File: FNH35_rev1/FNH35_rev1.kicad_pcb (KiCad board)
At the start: 2 copper layers, 13 x 7.7 mm, 118 parts, among them J1 Conn_01x03, J2 Conn_01x21, J3 DX07B024JJ3R1600, K0 KEYSW, K1 KEYSW, K10 KEYSW, K11 KEYSW, K12 KEYSW, K2 KEYSW, K20 KEYSW, K21 KEYSW, K22 KEYSW, K23 KEYSW, K30 KEYSW, K31 KEYSW, K32 KEYSW, K33 KEYSW, K40 KEYSW, K41 KEYSW, K42 KEYSW, K43 KEYSW, SW1 SW_PUSH, U1 STM32F303CCTx, U2 LD1117S33TR_SOT223, U3 74AHCT125, X1 XTAL_GND

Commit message: more pcb layouting, decided to get rid of fuse in next step
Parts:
- CB0, CB1, CB10, CB11, CB12, CB2, CB20, CB21, CB22, CB23, CB30, CB31, CB32, CB33, CB40, CB41, CB42, CB43, CU1, CU2, CU3, CU4, CU5, CU6, CU7, CU8, DS0, DS1, DS10, DS11, DS12, DS2, DS20, DS21, DS22, DS23, DS30, DS31, DS32, DS33, DS40, DS41, DS42, DS43, DU1, DU2, DU3, DU4, DU5, DU6, DU7, DU8, J2, J3: moved to B.Cu
- moved U2 194.3 mm to (26.2, 38.1), turned to 180 degrees
- moved C9 192.0 mm to (33.3, 31.0)
- moved C10 183.7 mm to (65.4, 21.4)
- moved C4 183.6 mm to (26.2, 45.2), turned to 90 degrees
- moved C3 182.9 mm to (33.3, 33.3)
- moved J3 179.5 mm to (27.1, 26.2)
- moved C11 162.1 mm to (26.2, 59.5), turned to 180 degrees
- moved X1 162.1 mm to (31.0, 87.3)
- moved U1 162.0 mm to (31.0, 73.8), turned to 90 degrees
- moved C1 156.6 mm to (40.5, 95.2), turned to 315 degrees
- moved C8 156.5 mm to (39.3, 69.1)
- moved C7 156.0 mm to (26.2, 64.3), turned to 90 degrees
- moved C2 154.6 mm to (45.2, 90.5), turned to 315 degrees
- moved C6 154.2 mm to (21.4, 78.6), turned to 180 degrees
- moved C5 153.7 mm to (24.9, 81.0), turned to 180 degrees
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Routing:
- added copper zone on B.Cu, net GNDD
- added copper zone on F.Cu, net GNDD
- removed copper zone on B.Cu, net +5V
- removed copper zone on F.Cu, net GND
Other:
- outline, holes or cut-outs redrawn

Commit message: almost done
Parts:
- removed F1: Polyfuse_Small, Capacitors_SMD:C_0805_HandSoldering
- removed JP1: , Wire_Connections_Bridges:WireConnection_1.00mmDrill
- C10, C3, C4, C9, D1, J1, R1, R2, U2: moved to B.Cu
- moved J1 187.7 mm to (26.2, 28.6), turned to 180 degrees
- moved R6 165.8 mm to (39.8, 74.6)
- moved D1 160.2 mm to (41.5, 32.4), turned to 45 degrees
- moved R7 157.1 mm to (41.2, 78.4), turned to 180 degrees
- moved R2 140.2 mm to (47.4, 35.2), turned to 180 degrees
- moved R1 140.0 mm to (47.5, 37.8), turned to 180 degrees
- moved U3 133.1 mm to (36.9, 40.3)
- moved SW1 118.1 mm to (22.1, 79.7), turned to 90 degrees
- moved R5 117.6 mm to (20.9, 87.3), turned to 180 degrees
- moved R3 112.1 mm to (8.02, 95.2)
- moved R4 111.9 mm to (1.03, 95.2)
- moved C10 33.9 mm to (33.5, 32.7), turned to 90 degrees
- moved C5 19.5 mm to (20.8, 61.9), turned to 270 degrees
- moved J3 16.7 mm to (43.7, 26.2)
- moved C1 16.2 mm to (27.1, 86.0)
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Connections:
- C1 pad 2: GNDD -> GND
- C11 pad 2: GNDD -> GND
- C12 pad 2: GNDD -> GND
- C2 pad 2: GNDD -> GND
- C3 pad 2: GNDD -> GND
- C4 pad 2: GNDD -> GND
- C5 pad 2: GNDD -> GND
- C6 pad 2: GNDD -> GND
- C7 pad 2: GNDD -> GND
- C8 pad 2: GNDD -> GND
- C9 pad 2: GNDD -> GND
- D1 pad 4: Net-(D1-Pad4) -> +5V
- J2 pad 13: Net-(J2-Pad13) -> /DA-
- J2 pad 14: Net-(J2-Pad14) -> /DA+
- J2 pad 20: GNDD -> GND
- J3 pad A4: Net-(D1-Pad4) -> +5V
- J3 pad A9: Net-(D1-Pad4) -> +5V
- J3 pad B4: Net-(D1-Pad4) -> +5V
- J3 pad B9: Net-(D1-Pad4) -> +5V
- R5 pad 2: GNDD -> GND
- U1 pad 23: GNDD -> GND
- U1 pad 32: Net-(J2-Pad13) -> /DA-
- U1 pad 33: Net-(J2-Pad14) -> /DA+
- U1 pad 35: GNDD -> GND
- U1 pad 47: GNDD -> GND
- U1 pad 8: GNDD -> GND
- U2 pad 1: GNDD -> GND
- X1 pad 3: GNDD -> GND
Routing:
- net +5V: track 0.00 -> 539.2 mm, vias 0 -> 30
- net GND: track 0.00 -> 538.5 mm, vias 0 -> 36
- net /SwitchMatrix/col3: track 0.00 -> 203.6 mm, vias 0 -> 7
- net /SwitchMatrix/col2: track 0.00 -> 183.9 mm, vias 0 -> 8
- net /SwitchMatrix/col0: track 0.00 -> 150.3 mm, vias 0 -> 7
- net /SwitchMatrix/row0: track 0.00 -> 141.8 mm, vias 0 -> 3
- net /SwitchMatrix/row1: track 0.00 -> 139.5 mm, vias 0 -> 1
- net /SwitchMatrix/col4: track 0.00 -> 136.4 mm, vias 0 -> 3
- net /SwitchMatrix/row2: track 0.00 -> 132.5 mm, vias 0 -> 1
- net /SwitchMatrix/row3: track 0.00 -> 85.2 mm, vias 0 -> 1
- net +3V3: track 0.00 -> 82.8 mm, vias 0 -> 1
- net Net-(DB23-Pad1): track 0.00 -> 60.5 mm
- net /SwitchMatrix/col1: track 0.00 -> 44.3 mm, vias 0 -> 4
- net Net-(DB11-Pad6): track 0.00 -> 43.8 mm, vias 0 -> 2
- net Net-(DB23-Pad6): track 0.00 -> 36.9 mm
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- added copper zone on B.Cu, net GND
- added copper zone on F.Cu, net GND
- removed copper zone on B.Cu, net GNDD
- removed copper zone on F.Cu, net GNDD
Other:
- outline, holes or cut-outs redrawn

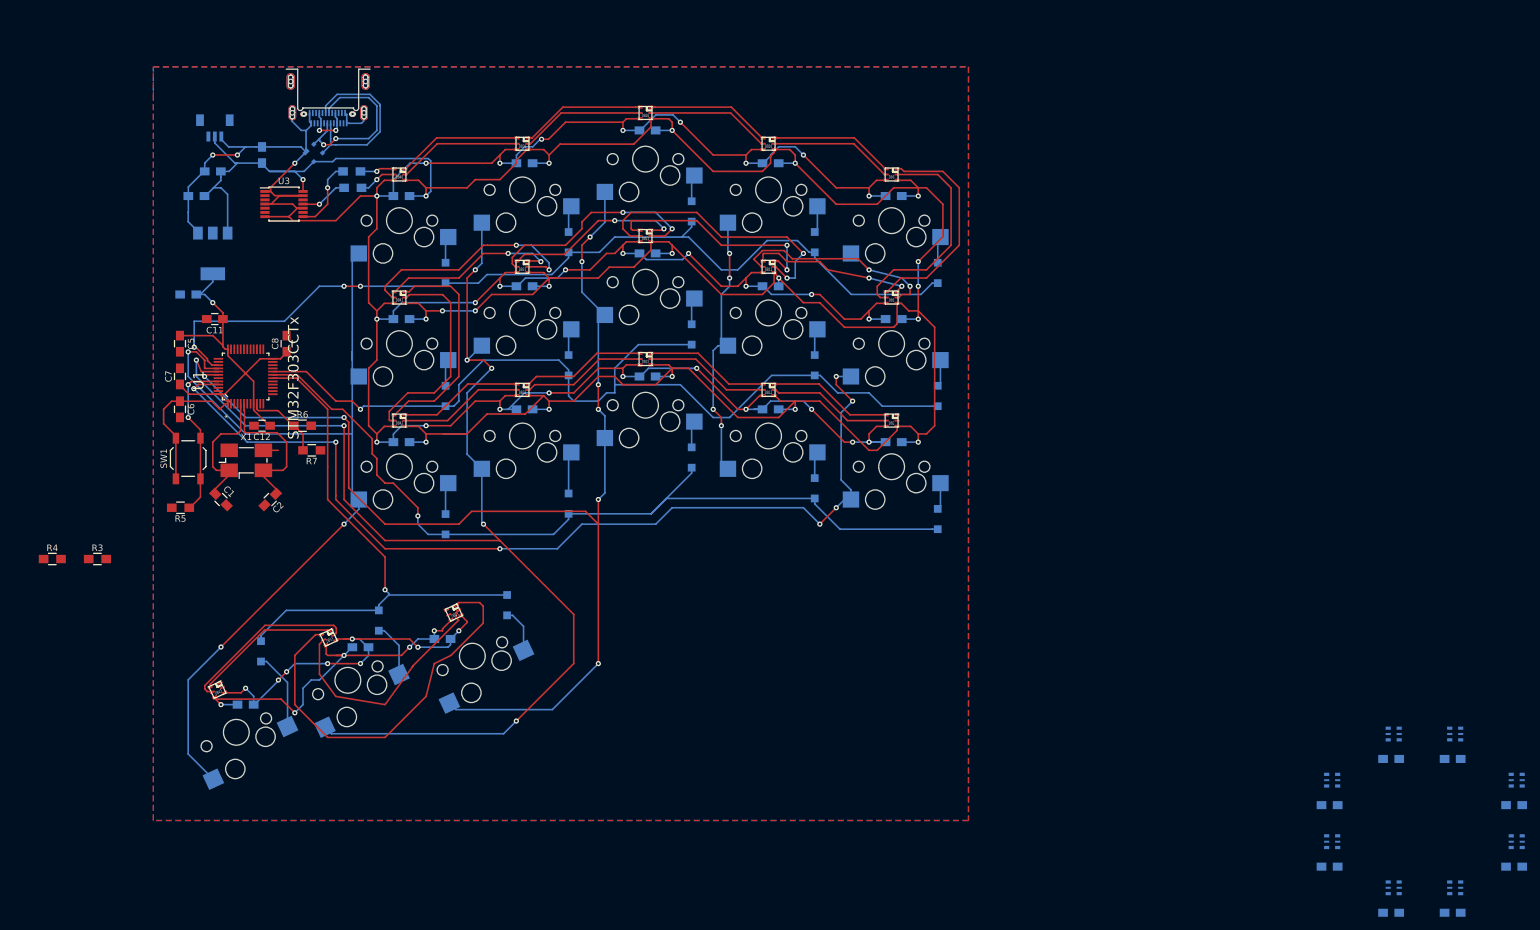
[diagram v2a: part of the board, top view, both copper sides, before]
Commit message: noticed the diodes are conflicting with the sockets, deleting traces from here
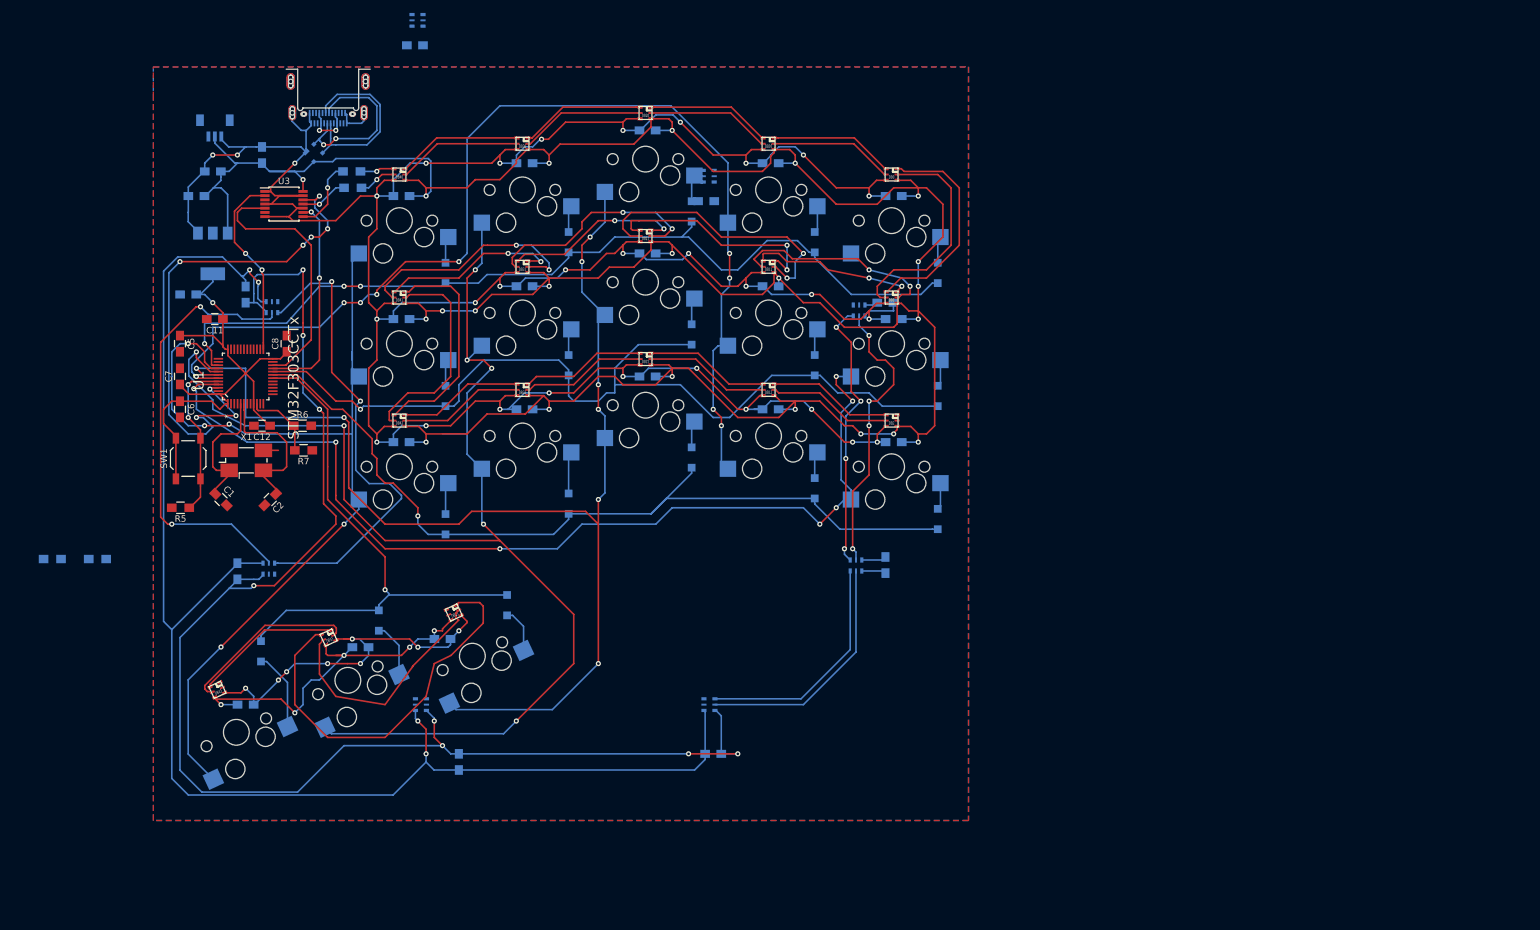
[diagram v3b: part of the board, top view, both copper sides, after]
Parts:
- R3, R4: moved to B.Cu
- moved CU1 187.2 mm to (57.2, 15.7)
- moved DU1 187.2 mm to (57.6, 11.9)
- moved CU5 185.5 mm to (31.0, 54.3), turned to 270 degrees
- moved DU8 179.7 mm to (35.0, 56.3), turned to 90 degrees
- moved CU6 175.2 mm to (29.7, 97.1), turned to 270 degrees
- moved DU7 170.0 mm to (34.6, 96.7), turned to 90 degrees
- moved DU6 153.2 mm to (58.1, 117.8), turned to 180 degrees
- moved CU7 146.2 mm to (64.0, 126.7), turned to 90 degrees
- moved CU2 144.3 mm to (102.3, 39.8)
- moved DU2 144.3 mm to (102.7, 36.0)
- moved DU3 125.1 mm to (125.9, 56.8), turned to 270 degrees
- moved CU3 124.6 mm to (130.0, 55.6)
- moved DU5 118.9 mm to (102.8, 117.8), turned to 180 degrees
- moved CU8 117.1 mm to (103.3, 125.4)
- moved DU4 110.9 mm to (125.5, 96.3), turned to 270 degrees
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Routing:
- net +5V: track 539.2 -> 772.2 mm, vias 30 -> 36
- net GND: track 538.5 -> 765.1 mm, vias 36 -> 44
- net /SwitchMatrix/col1: track 44.3 -> 174.7 mm, vias 4 -> 9
- net Net-(U1-Pad46): track 0.00 -> 83.4 mm, vias 0 -> 8
- net Net-(DU7-Pad1): track 0.00 -> 74.6 mm, vias 0 -> 2
- net Net-(DU7-Pad6): track 0.00 -> 68.1 mm, vias 0 -> 2
- net Net-(DU3-Pad6): track 0.00 -> 44.3 mm, vias 0 -> 4
- net Net-(DU3-Pad1): track 0.00 -> 42.4 mm, vias 0 -> 4
- net Net-(U1-Pad22): track 0.00 -> 41.0 mm
- net Net-(DU4-Pad6): track 0.00 -> 37.8 mm
- net Net-(DU4-Pad1): track 0.00 -> 36.3 mm
- net Net-(U1-Pad21): track 0.00 -> 32.5 mm, vias 0 -> 2
- net Net-(U1-Pad25): track 0.00 -> 28.9 mm, vias 0 -> 2
- net /SwitchMatrix/col4: track 136.4 -> 145.5 mm, vias 3 -> 5
- net /SwitchMatrix/col2: track 183.9 -> 191.8 mm
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
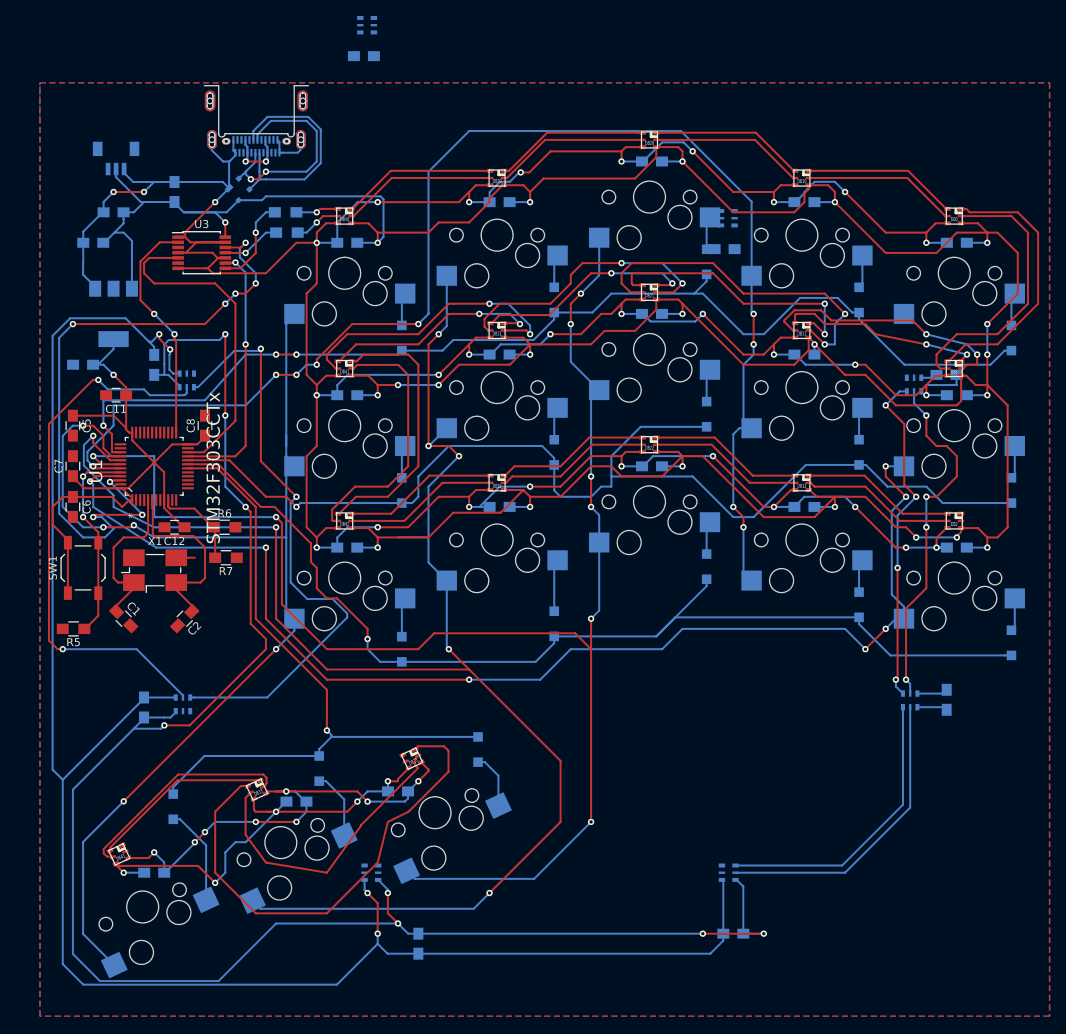
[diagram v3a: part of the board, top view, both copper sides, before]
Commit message: routed backlight data
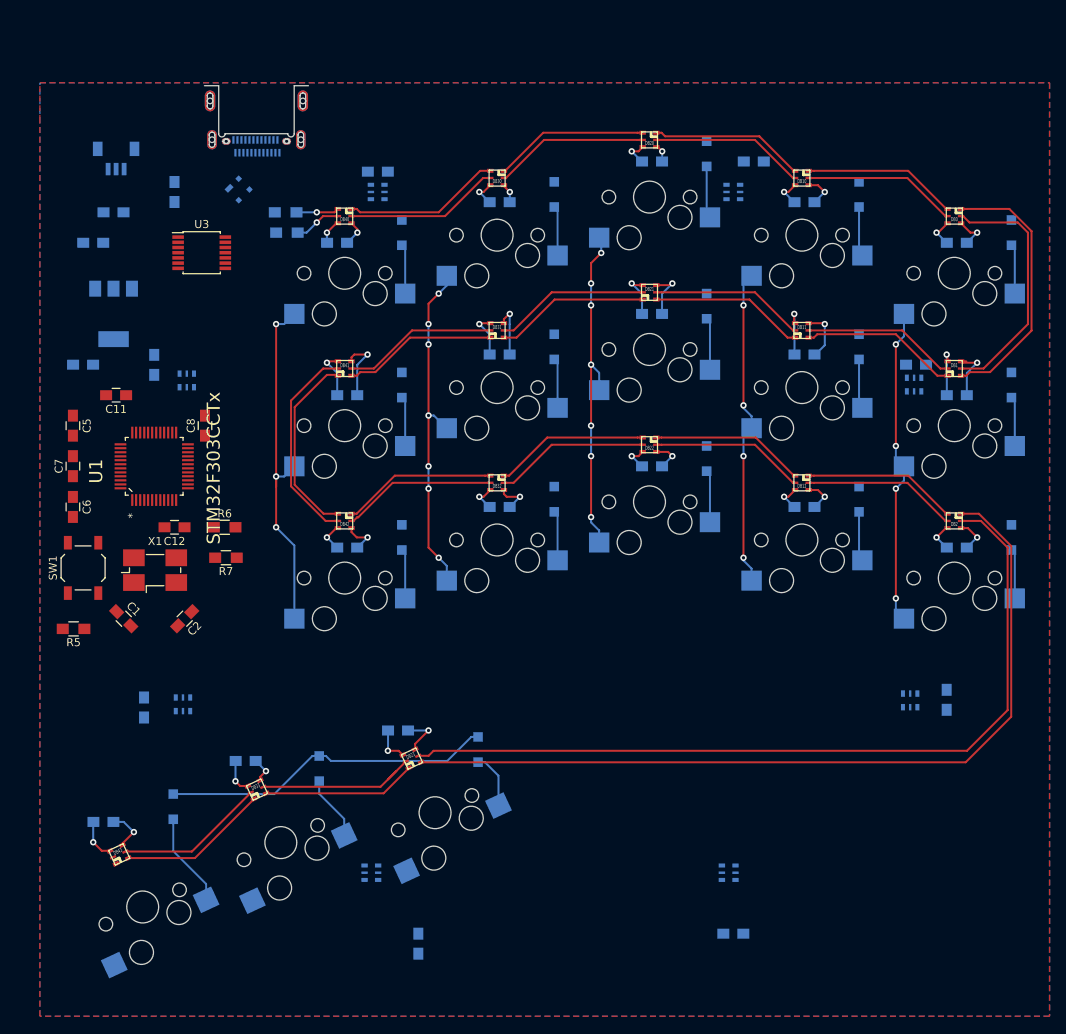
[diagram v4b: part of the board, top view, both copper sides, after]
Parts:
- moved DU1 20.9 mm to (58.9, 32.7)
- moved DS32 15.6 mm to (81.0, 71.1), turned to 270 degrees
- moved CU1 14.6 mm to (58.9, 30.2)
- moved DS42 14.0 mm to (61.9, 75.9), turned to 270 degrees
- moved DS20 13.5 mm to (100.0, 27.9), turned to 270 degrees
- moved DS21 13.5 mm to (100.0, 47.0), turned to 270 degrees
- moved DS22 13.5 mm to (100.0, 66.0), turned to 270 degrees
- moved DS11 13.2 mm to (119.1, 52.1), turned to 270 degrees
- moved DS31 13.2 mm to (81.0, 52.1), turned to 270 degrees
- moved DS10 13.2 mm to (119.1, 33.0), turned to 270 degrees
- moved DS12 13.2 mm to (119.1, 71.1), turned to 270 degrees
- moved DS30 13.2 mm to (81.0, 33.0), turned to 270 degrees
- moved DS2 13.2 mm to (138.1, 75.9), turned to 270 degrees
- moved DS0 13.2 mm to (138.1, 37.8), turned to 270 degrees
- moved DS1 13.2 mm to (138.1, 56.8), turned to 270 degrees
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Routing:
- net +5V: track 772.2 -> 82.0 mm, vias 36 -> 18
- net GND: track 765.1 -> 84.3 mm, vias 44 -> 18
- net /SwitchMatrix/col3: track 207.5 -> 42.9 mm
- net /SwitchMatrix/col2: track 191.8 -> 42.7 mm, vias 8 -> 7
- net /SwitchMatrix/row1: track 139.5 -> 0.00 mm, vias 1 -> 0
- net /SwitchMatrix/row0: track 139.4 -> 0.00 mm, vias 3 -> 0
- net /SwitchMatrix/col1: track 174.7 -> 39.8 mm, vias 9 -> 4
- net /SwitchMatrix/row2: track 132.5 -> 0.00 mm, vias 1 -> 0
- net /SwitchMatrix/col0: track 151.3 -> 39.8 mm, vias 7 -> 4
- net Net-(DB2-Pad1): track 0.00 -> 105.4 mm
- net Net-(DB2-Pad6): track 0.00 -> 103.6 mm
- net /SwitchMatrix/col4: track 145.5 -> 44.7 mm, vias 5 -> 3
- net Net-(U1-Pad46): track 83.4 -> 0.00 mm, vias 8 -> 0
- net +3V3: track 82.8 -> 0.00 mm, vias 1 -> 0
- net Net-(DU7-Pad1): track 74.6 -> 0.00 mm, vias 2 -> 0
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
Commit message: pcb finished. Next up: review and left hand
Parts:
- J2: value Conn_01x21 -> Conn_01x08; footprint Pin_Headers:Pin_Header_Angled_1x21_Pitch2.54mm -> Pin_Headers:Pin_Header_Angled_1x08_Pitch1.27mm
- J3: footprint DX07B024JJ3R1600:JAE_DX07B024JJ3R1600 -> butts:JAE_DX07B024JJ3R1600
- moved J2 115.8 mm to (100.8, 107.6), turned to 0 degrees
- moved R4 56.6 mm to (37.3, 51.8), turned to 180 degrees
- moved R3 56.5 mm to (37.3, 47.0), turned to 180 degrees
- moved R5 33.5 mm to (40.5, 60.1), turned to 0 degrees
- moved C11 32.5 mm to (35.2, 89.3)
- moved C5 30.8 mm to (40.6, 85.5), turned to 90 degrees
- moved C8 27.1 mm to (24.1, 85.5), turned to 270 degrees
- moved C2 26.0 mm to (26.6, 61.4), turned to 45 degrees
- moved C1 25.7 mm to (34.2, 61.4), turned to 135 degrees
- moved C7 23.9 mm to (40.6, 80.4), turned to 270 degrees
- moved SW1 21.0 mm to (39.3, 67.7), turned to 270 degrees
- moved R7 20.7 mm to (21.5, 69.0), turned to 0 degrees
- moved R6 18.2 mm to (21.6, 72.8), turned to 180 degrees
- moved C6 16.8 mm to (37.3, 75.3), turned to 90 degrees
- moved U1 13.4 mm to (30.4, 80.4), turned to 270 degrees
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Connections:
- J2 pad 6: Net-(J2-Pad6) -> /PB13
- J2 pad 7: Net-(J2-Pad7) -> /PB14
- J2 pad 8: Net-(J2-Pad8) -> +3V3
- J3 pad B6: /DA+ -> Net-(J3-PadB6)
- J3 pad B7: /DA- -> Net-(J3-PadB7)
- U1 pad 14: Net-(J2-Pad6) -> Net-(U1-Pad14)
- U1 pad 15: Net-(J2-Pad7) -> Net-(U1-Pad15)
- U1 pad 16: Net-(J2-Pad8) -> Net-(U1-Pad16)
- U1 pad 17: Net-(J2-Pad9) -> Net-(U1-Pad17)
- U1 pad 28: /SerComm -> /SerConn
- U1 pad 29: Net-(J2-Pad10) -> Net-(U1-Pad29)
- U1 pad 30: Net-(J2-Pad11) -> Net-(U1-Pad30)
- U1 pad 31: Net-(J2-Pad12) -> Net-(U1-Pad31)
- U1 pad 34: Net-(J2-Pad15) -> Net-(U1-Pad34)
- U1 pad 37: Net-(J2-Pad16) -> Net-(U1-Pad37)
- U1 pad 38: Net-(J2-Pad17) -> Net-(U1-Pad38)
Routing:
- net GND: track 84.3 -> 966.1 mm, vias 18 -> 54
- net +5V: track 82.0 -> 848.1 mm, vias 18 -> 52
- net /SwitchMatrix/row0: track 0.00 -> 192.5 mm, vias 0 -> 9
- net /SwitchMatrix/row1: track 0.00 -> 184.8 mm, vias 0 -> 11
- net /SwitchMatrix/row2: track 0.00 -> 180.4 mm, vias 0 -> 9
- net +3V3: track 0.00 -> 168.0 mm, vias 0 -> 4
- net /SwitchMatrix/col0: track 39.8 -> 153.9 mm, vias 4 -> 10
- net /SwitchMatrix/col2: track 42.7 -> 154.2 mm, vias 7 -> 13
- net Net-(J2-Pad3): track 0.00 -> 108.1 mm, vias 0 -> 3
- net Net-(J2-Pad4): track 0.00 -> 102.7 mm, vias 0 -> 3
- net /SerConn: track 0.00 -> 97.4 mm, vias 0 -> 7
- net Net-(J2-Pad5): track 0.00 -> 93.3 mm, vias 0 -> 5
- net Net-(DU6-Pad6): track 0.00 -> 87.6 mm
- net /PB13: track 0.00 -> 87.3 mm, vias 0 -> 3
- net /PB14: track 0.00 -> 85.2 mm, vias 0 -> 3
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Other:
- board size 13 x 7.7 mm -> 126.2 x 116.7 mm
